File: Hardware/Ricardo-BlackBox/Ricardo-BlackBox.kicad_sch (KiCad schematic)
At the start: 43 parts, among them IC1 XTSD08GLGEAG, J1 RBUS, U1 ESP32-S3, Y1 40MHz±10ppm

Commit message: Initial hardware update
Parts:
- removed C12: 4.2pF, Capacitor_SMD:C_0402_1005Metric, symbol Device:C_Small
- removed C28: 10uF, Capacitor_SMD:C_0402_1005Metric, symbol Device:C_Small
- removed IC1: XTSD08GLGEAG, iclr:SOTFL50P160X60-8N, symbol chest:XTSD08GLGEAG
- removed TP11, TP12, TP13, TP14: TestPoint, TestPoint:TestPoint_Pad_D1.0mm, symbol Connector:TestPoint
- added C12: 10uF, Capacitor_SMD:C_0402_1005Metric, symbol Device:C
- added C18: 0.1uF, Capacitor_SMD:C_0402_1005Metric, symbol Device:C
- added CRXLED1: ORANGE_LED, Resistor_SMD:R_0402_1005Metric, symbol Device:LED_Small
- added CTXLED1: GREEN_LED, Resistor_SMD:R_0402_1005Metric, symbol Device:LED_Small
- added J3: Conn_02x04_Odd_Even, Connector_PinHeader_2.54mm:PinHeader_2x04_P2.54mm_Vertical, symbol Connector_Generic:Conn_02x04_Odd_Even
- added J4: Conn_02x03_Odd_Even, Connector_PinHeader_2.54mm:PinHeader_2x03_P2.54mm_Vertical, symbol Connector_Generic:Conn_02x03_Odd_Even
- added R18: 1k, Resistor_SMD:R_0402_1005Metric, symbol Device:R_Small
- added R19, R20: 10K, Resistor_SMD:R_0402_1005Metric, symbol Device:R
- added U6: XTSD08G, Package_LGA:LGA-8_8x6mm_P1.27mm, symbol Memory_Flash:XTSD08G
- added U7: LM66200DRLR, SOTFL50P160X60-8N, symbol iclr:LM66200DRLR
- added U8: SN74CBTLV3245APWR, SN74CBTLV3245APWR:SOP65P640X120-20N, symbol SN74CBTLV3245APWR:SN74CBTLV3245APWR
- 12VLED1: value 12V_LED -> RED_LED
- 3V3LED1: value 3V3LED -> BLUE_LED
- C13, C14: value C -> 11pF
- R5: value 47.5 -> 1k
- R6: value 499 -> 499R
- TXLED1: value TX_LED -> GREEN_LED
- U1: footprint Package_DFN_QFN:QFN-56-1EP_7x7mm_P0.4mm_EP5.6x5.6mm -> iclr:QFN40P700X700X90-57N
- Y1: value 40MHz±10ppm -> R940000171
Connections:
- net +3V3: now also R5.1, J4.2 (Pin_2), R18.1, R19.2, R20.1, U7.3 (VIN1), U8.19 (~{OE}), U8.20 (VCC)
- net CAN_RX: now also U1.7 (GPIO2/ADC1_CH1), CRXLED1.1 (K)
- net CAN_TX: now also U1.6 (GPIO1/ADC1_CH0), CTXLED1.1 (K)
- net GND: now also C12.2, C18.2, J3.1 (Pin_1), J4.1 (Pin_1), R20.2, U6.4 (VSS), U7.1 (GND_1), U7.4 (~{ON}), U7.5 (GND_2), U8.10 (GND); no longer R5.1
- net RXD: now also U1.50 (U0RXD/PROG/GPIO44); no longer R6.1
- net TXD: now also R6.1; no longer U1.50 (U0RXD/PROG/GPIO44)
- net at R5.2: now also CTXLED1.2 (A)
- net GPIO_5: now reaches U1.10 (GPIO5/ADC1_CH4)
- net GPIO_5: now also J4.4 (Pin_4)
- net GPIO_6: now reaches U1.11 (GPIO6/ADC1_CH5)
- net GPIO_6: now also J4.5 (Pin_5)
- net GPIO_7: now reaches U1.12 (GPIO7/ADC1_CH6)
- net GPIO_7: now also J4.6 (Pin_6)
- net NAND_SD2: now reaches U1.37 (SPICLK_P/GPIO47)
- net NAND_SD2: now also U6.1 (SD2), U8.13 (B6)
- net NAND_SD3: now reaches U1.38 (GPIO33)
- net NAND_SD3: now also U6.2 (SD3/~{CS}), U8.14 (B5)
- net NAND_CLK: now reaches U1.39 (GPIO34)
- net NAND_CLK: now also U6.3 (CLK), U8.15 (B4)
- net GPIO_4: now reaches U1.9 (GPIO4/ADC1_CH3)
- net GPIO_4: now also J4.3 (Pin_3)
- net CLK renamed NAND_SD0
- net NAND_SD0: now also U6.6 (SD0/DO), U8.17 (B2)
- net MISO renamed NAND_SD1
- net NAND_SD1: now also U6.7 (SD1), U8.18 (B1)
- net MOSI: no longer names the net of U1.43 (GPIO38)
- net NAND_CS renamed NAND_CMD
- net NAND_CMD: now also U6.5 (CMD/DI), U8.16 (B3)
- new net: CRXLED1.2 (A), R18.2
- new net: R19.1, U7.8 (ST)
- new net HEADER_3V3: J3.2 (Pin_2), U7.6 (VIN2)
- new net HEADER_CLK: J3.5 (Pin_5), U8.5 (A4)
- new net HEADER_CMD: J3.6 (Pin_6), U8.4 (A3)
- new net HEADER_SD0: J3.3 (Pin_3), U8.3 (A2)
- new net HEADER_SD1: J3.4 (Pin_4), U8.2 (A1)
- new net HEADER_SD2: J3.7 (Pin_7), U8.7 (A6)
- new net HEADER_SD3: J3.8 (Pin_8), U8.6 (A5)
- new net NAND_3V3: C12.1, C18.1, U6.8 (VDD), U7.2 (VOUT_1), U7.7 (VOUT_2)
- no-connect marks 36 -> 15
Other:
- sheet USB -> UART renamed USB
- sheet USB: file usb-uart.kicad_sch -> usb.kicad_sch
- sheet USB ports: added none; removed 3.3V
- note added: "GPIO Breakout"
- note added: "NAND 3V3 Switching"
- note added: "NAND Data Isolation"
- note added: "NAND Flash"
- note added: "NAND Header"
- note added: "Reserved for integrated flash"
- note removed: "TBD C and R value to get a total series impedance of 50 ohms at 2.4GHz"
- moved on the sheet: TP10, TP9

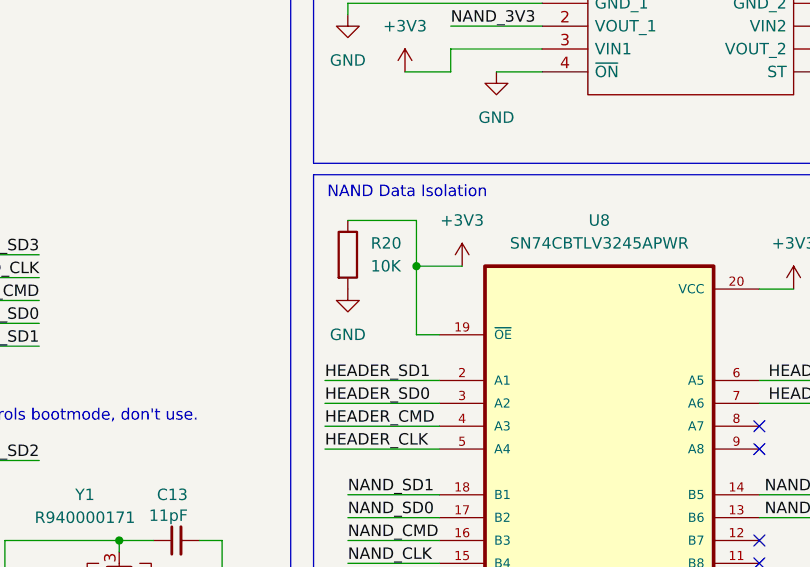
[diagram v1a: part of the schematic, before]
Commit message: Moved decoupling capacitors
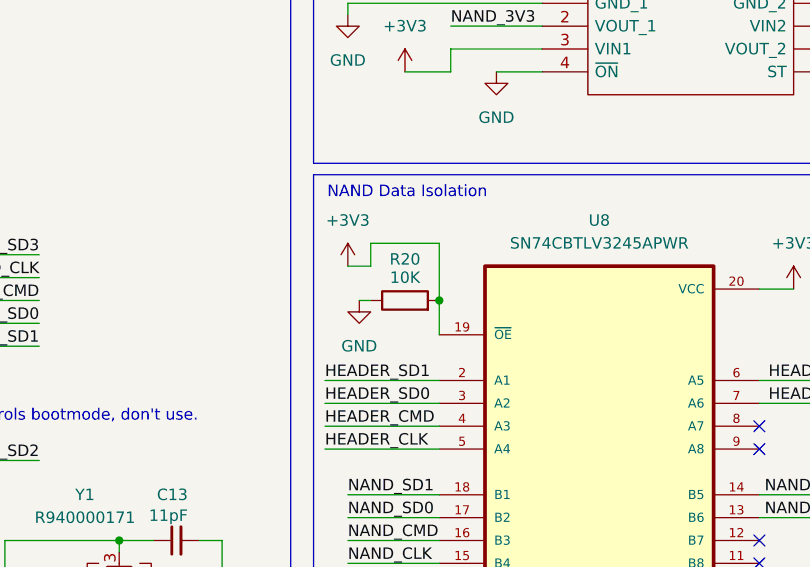
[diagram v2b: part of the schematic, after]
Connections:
- net +3V3: now also R20.2; no longer R20.1
- net GND: now also R20.1; no longer R20.2
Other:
- moved on the sheet: R20
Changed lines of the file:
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@@
 	)
 	(junction
-		(at 189.23 96.52)
-		(diameter 0)
-		(color 0 0 0 0)
-	)
-	(junction
 		(at 34.29 135.89)
 		(diameter 0)
@@
 	)
 	(junction
+		(at 191.77 100.33)
+		(diameter 0)
+		(color 0 0 0 0)
+	)
+	(junction
 		(at 29.21 140.97)
 		(diameter 0)
@@
 	(wire
 		(pts
+			(xy 191.77 100.33) (xy 191.77 104.14)
+		)
+		(stroke
+			(width 0)
+			(type default)
+		)
+	)
+	(wire
+		(pts
 			(xy 30.48 191.77) (xy 30.48 190.5)
 		)
@@
 	(wire
 		(pts
-			(xy 179.07 116.84) (xy 191.77 116.84)
+			(xy 184.15 93.98) (xy 191.77 93.98)
 		)
 		(stroke
@@
 	(wire
 		(pts
-			(xy 29.21 135.89) (xy 34.29 135.89)
+			(xy 179.07 116.84) (xy 191.77 116.84)
 		)
 		(stroke
@@
 	(wire
 		(pts
-			(xy 181.61 129.54) (xy 191.77 129.54)
+			(xy 29.21 135.89) (xy 34.29 135.89)
 		)
 		(stroke
@@
 	(wire
 		(pts
-			(xy 135.89 105.41) (xy 147.32 105.41)
+			(xy 181.61 129.54) (xy 191.77 129.54)
 		)
 		(stroke
@@
 	(wire
 		(pts
-			(xy 236.22 72.39) (xy 246.38 72.39)
+			(xy 135.89 105.41) (xy 147.32 105.41)
 		)
 		(stroke
@@
 	(wire
 		(pts
-			(xy 143.51 138.43) (xy 156.21 138.43)
+			(xy 236.22 72.39) (xy 246.38 72.39)
 		)
 		(stroke
@@
 	(wire
 		(pts
-			(xy 194.31 96.52) (xy 189.23 96.52)
+			(xy 143.51 138.43) (xy 156.21 138.43)
 		)
 		(stroke
@@
 		)
 	)
-	(wire
-		(pts
-			(xy 181.61 91.44) (xy 189.23 91.44)
-		)
-		(stroke
-			(width 0)
-			(type default)
-		)
-	)
 	(polyline
 		(pts
@@
 	(wire
 		(pts
-			(xy 189.23 104.14) (xy 191.77 104.14)
-		)
-		(stroke
-			(width 0)
-			(type default)
-		)
-	)
-	(wire
-		(pts
 			(xy 236.22 31.75) (xy 240.03 31.75)
 		)
@@
 	(wire
 		(pts
+			(xy 184.15 96.52) (xy 181.61 96.52)
+		)
+		(stroke
+			(width 0)
+			(type default)
+		)
+	)
+	(wire
+		(pts
 			(xy 227.33 99.06) (xy 231.14 99.06)
 		)
@@
 	(wire
 		(pts
-			(xy 189.23 91.44) (xy 189.23 96.52)
+			(xy 191.77 93.98) (xy 191.77 100.33)
 		)
 		(stroke
@@
 	(wire
 		(pts
-			(xy 189.23 96.52) (xy 189.23 104.14)
-		)
-		(stroke
-			(width 0)
-			(type default)
-		)
-	)
-	(wire
-		(pts
 			(xy 236.22 74.93) (xy 238.76 74.93)
 		)
@@
 	(wire
 		(pts
+			(xy 184.15 93.98) (xy 184.15 96.52)
+		)
+		(stroke
+			(width 0)
+			(type default)
+		)
+	)
+	(wire
+		(pts
 			(xy 143.51 127) (xy 156.21 127)
 		)
@@
 	(wire
 		(pts
+			(xy 182.88 100.33) (xy 184.15 100.33)
+		)
+		(stroke
+			(width 0)
+			(type default)
+		)
+	)
+	(wire
+		(pts
 			(xy 45.72 182.88) (xy 45.72 185.42)
 		)
@@
 		(lib_name "GND_7")
 		(lib_id "power:GND")
-		(at 181.61 99.06 0)
+		(at 182.88 100.33 0)
 		(unit 1)
 		(exclude_from_sim no)
@@
 		(fields_autoplaced yes)
 		(property "Reference" "#PWR059"
-			(at 181.61 105.41 0)
+			(at 182.88 106.68 0)
 			(effects
 				(font
@@
 		)
 		(property "Value" "GND"
-			(at 181.61 104.14 0)
+			(at 182.88 105.41 0)
 			(effects
 				(font
@@
 		)
 		(property "Footprint" ""
-			(at 181.61 99.06 0)
+			(at 182.88 100.33 0)
 			(effects
 				(font
@@
 		)
 		(property "Datasheet" ""
-			(at 181.61 99.06 0)
+			(at 182.88 100.33 0)
 			(effects
 				(font
@@
 		)
 		(property "Description" "Power symbol creates a global label with name \"GND\" , ground"
-			(at 181.61 99.06 0)
+			(at 182.88 100.33 0)
 			(effects
 				(font
@@
 		(lib_name "+3.3V_3")
 		(lib_id "power:+3.3V")
-		(at 194.31 96.52 0)
+		(at 181.61 96.52 0)
 		(unit 1)
 		(exclude_from_sim no)
@@
 		(fields_autoplaced yes)
 		(property "Reference" "#PWR057"
-			(at 194.31 100.33 0)
+			(at 181.61 100.33 0)
 			(effects
 				(font
@@
 		)
 		(property "Value" "+3V3"
-			(at 194.31 91.44 0)
+			(at 181.61 91.44 0)
 			(effects
 				(font
@@
 		)
 		(property "Footprint" ""
-			(at 194.31 96.52 0)
+			(at 181.61 96.52 0)
 			(effects
 				(font
@@
 		)
 		(property "Datasheet" ""
-			(at 194.31 96.52 0)
+			(at 181.61 96.52 0)
 			(effects
 				(font
@@
 		)
 		(property "Description" "Power symbol creates a global label with name \"+3.3V\""
-			(at 194.31 96.52 0)
+			(at 181.61 96.52 0)
 			(effects
 				(font
@@
 	(symbol
 		(lib_id "Device:R")
-		(at 181.61 95.25 0)
+		(at 187.96 100.33 90)
 		(unit 1)
 		(exclude_from_sim no)
@@
 		(on_board yes)
 		(dnp no)
-		(fields_autoplaced yes)
 		(property "Reference" "R20"
-			(at 184.15 93.9799 0)
+			(at 187.96 95.758 90)
 			(effects
 				(font
 					(size 1.27 1.27)
 				)
-				(justify left)
 			)
 		)
 		(property "Value" "10K"
-			(at 184.15 96.5199 0)
+			(at 187.96 97.79 90)
 			(effects
 				(font
 					(size 1.27 1.27)
 				)
-				(justify left)
 			)
 		)
 		(property "Footprint" "Resistor_SMD:R_0402_1005Metric"
-			(at 179.832 95.25 90)
+			(at 187.96 102.108 90)
 			(effects
 				(font
@@
 		)
 		(property "Datasheet" "~"
-			(at 181.61 95.25 0)
+			(at 187.96 100.33 0)
 			(effects
 				(font
@@
 		)
 		(property "Description" "Resistor"
-			(at 181.61 95.25 0)
+			(at 187.96 100.33 0)
 			(effects
 				(font

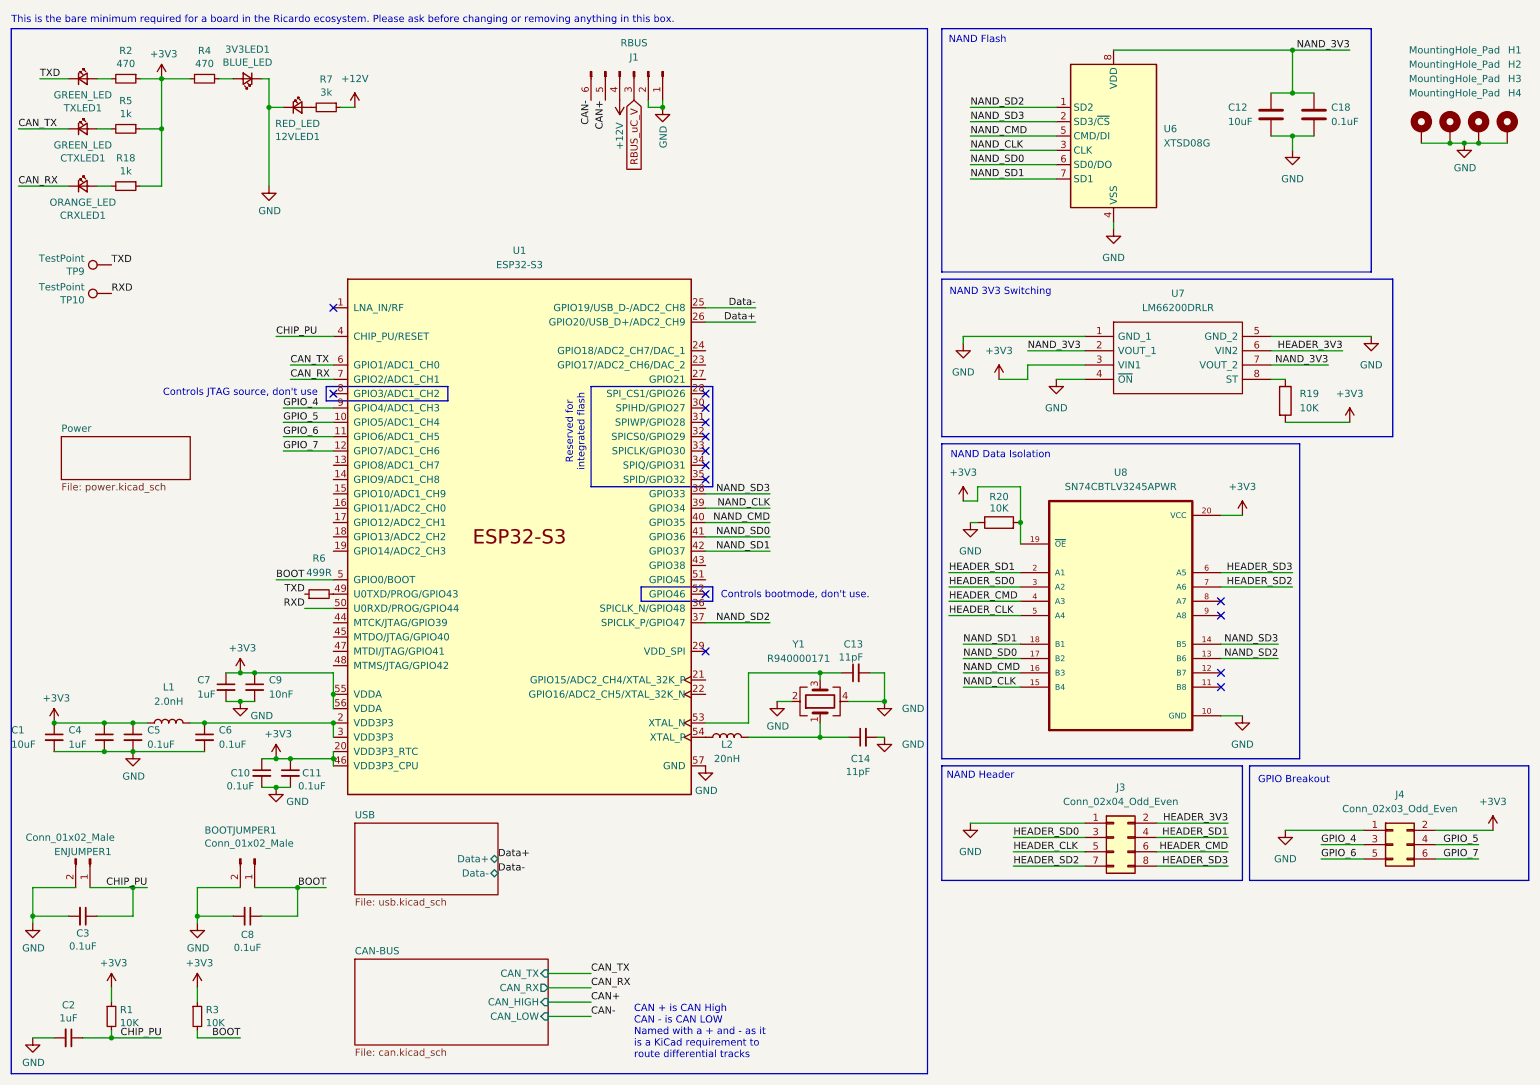
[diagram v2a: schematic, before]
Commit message: Removed data line switching and rearranged
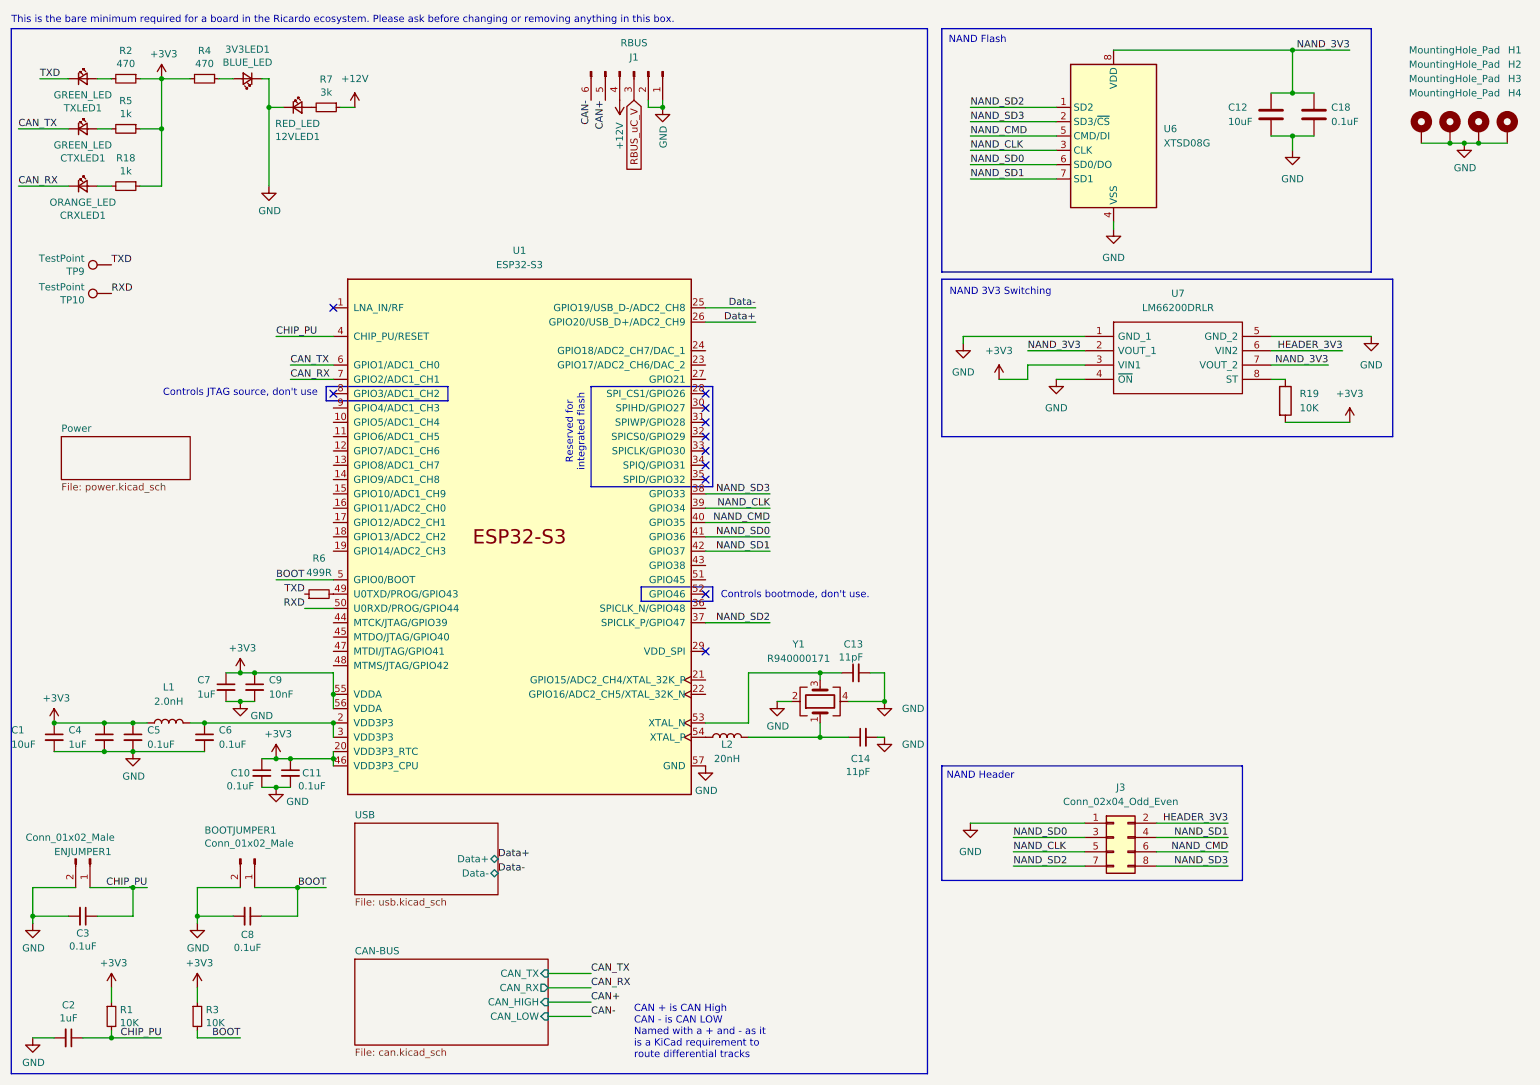
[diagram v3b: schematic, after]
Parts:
- removed J4: Conn_02x03_Odd_Even, Connector_PinHeader_2.54mm:PinHeader_2x03_P2.54mm_Vertical, symbol Connector_Generic:Conn_02x03_Odd_Even
- removed R20: 10K, Resistor_SMD:R_0402_1005Metric, symbol Device:R
- removed U8: SN74CBTLV3245APWR, SN74CBTLV3245APWR:SOP65P640X120-20N, symbol SN74CBTLV3245APWR:SN74CBTLV3245APWR
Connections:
- net HEADER_CLK is gone; now on net NAND_CLK: J3.5 (Pin_5)
- net HEADER_CMD is gone; now on net NAND_CMD: J3.6 (Pin_6)
- net HEADER_SD0 is gone; now on net NAND_SD0: J3.3 (Pin_3)
- net HEADER_SD1 is gone; now on net NAND_SD1: J3.4 (Pin_4)
- net HEADER_SD2 is gone; now on net NAND_SD2: J3.7 (Pin_7)
- net HEADER_SD3 is gone; now on net NAND_SD3: J3.8 (Pin_8)
- net GPIO_4: no longer names the net of U1.9 (GPIO4/ADC1_CH3)
- net GPIO_5: no longer names the net of U1.10 (GPIO5/ADC1_CH4)
- net GPIO_6: no longer names the net of U1.11 (GPIO6/ADC1_CH5)
- net GPIO_7: no longer names the net of U1.12 (GPIO7/ADC1_CH6)
- no-connect marks 15 -> 11
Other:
- note removed: "GPIO Breakout"
- note removed: "NAND Data Isolation"
